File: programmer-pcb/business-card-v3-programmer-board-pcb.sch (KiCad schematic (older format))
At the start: 18 parts, among them J1 Pogo_Pin_Conn, J2 Power_TP, J3 Programmer_Conn, J4 Jack-DC, SW1 RST, U1 LM2904, U2 L7805CV

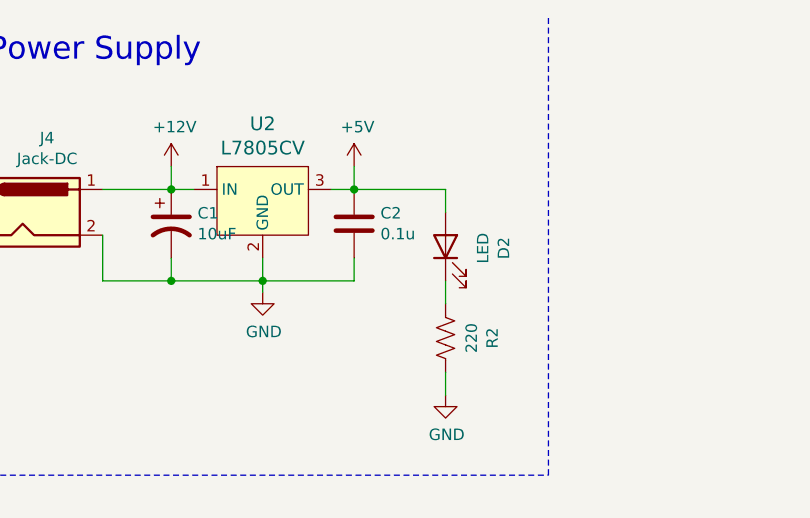
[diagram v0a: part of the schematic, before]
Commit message: remove the rescue lib folder
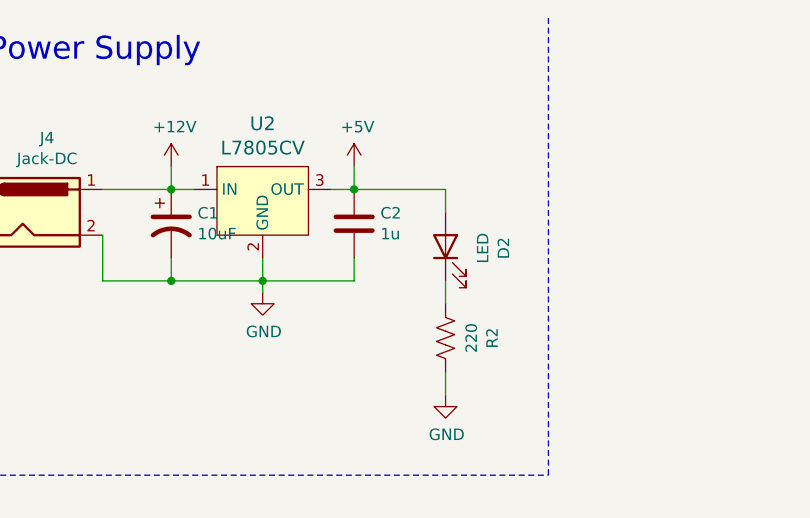
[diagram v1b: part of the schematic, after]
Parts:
- C2: value 0.1u -> 1u
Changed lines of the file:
@@
 P 2300 1400
 F 0 "C2" H 2415 1446 50  0000 L CNN
-F 1 "0.1u" H 2415 1355 50  0000 L CNN
+F 1 "1u" H 2415 1355 50  0000 L CNN
 F 2 "Capacitor_SMD:C_0603_1608Metric" H 2338 1250 50  0001 C CNN
 F 3 "~" H 2300 1400 50  0001 C CNN
